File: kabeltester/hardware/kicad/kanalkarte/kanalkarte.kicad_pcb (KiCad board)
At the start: 6 copper layers, 118 x 74 mm, 413 parts, among them J1 DIN 41612 C96 Feder, J2 Messkarte, U1 SN74HC595PW, U10 CD74HCT4067M96, U11 ADG1606BRUZ, U12 CD74HCT4067M96, U13 ADG1606BRUZ, U14 CD74HCT4067M96, U15 ADG1606BRUZ, U16 CD74HCT4067M96, U17 ADG1606BRUZ, U18 CD74HCT4067M96, U2 SN74HC595PW, U3 ADG1606BRUZ, U4 CD74HCT4067M96, U5 ADG1606BRUZ, U6 CD74HCT4067M96, U7 ADG1606BRUZ, U8 CD74HCT4067M96, U9 ADG1606BRUZ

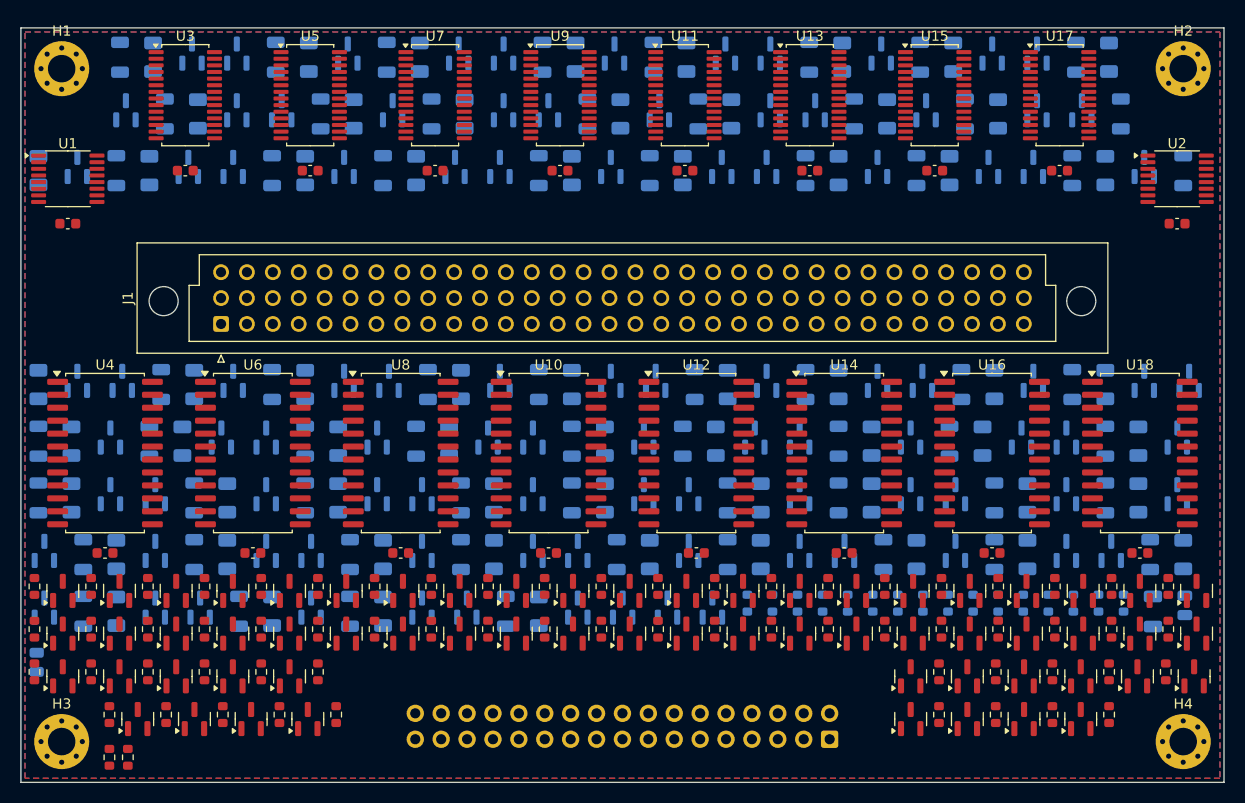
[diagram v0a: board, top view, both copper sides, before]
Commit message: Kanalkarte 6 Lagen, neue Platzierung: Zwischenstand Runde 1 (945 -> 180 offen)
Co-Authored-By: Claude Opus 5.5 <noreply@anthropic.com>
Claude-Session: https://claude.ai/code/session_0119zGeGQCWTR3UwpEi96iWe
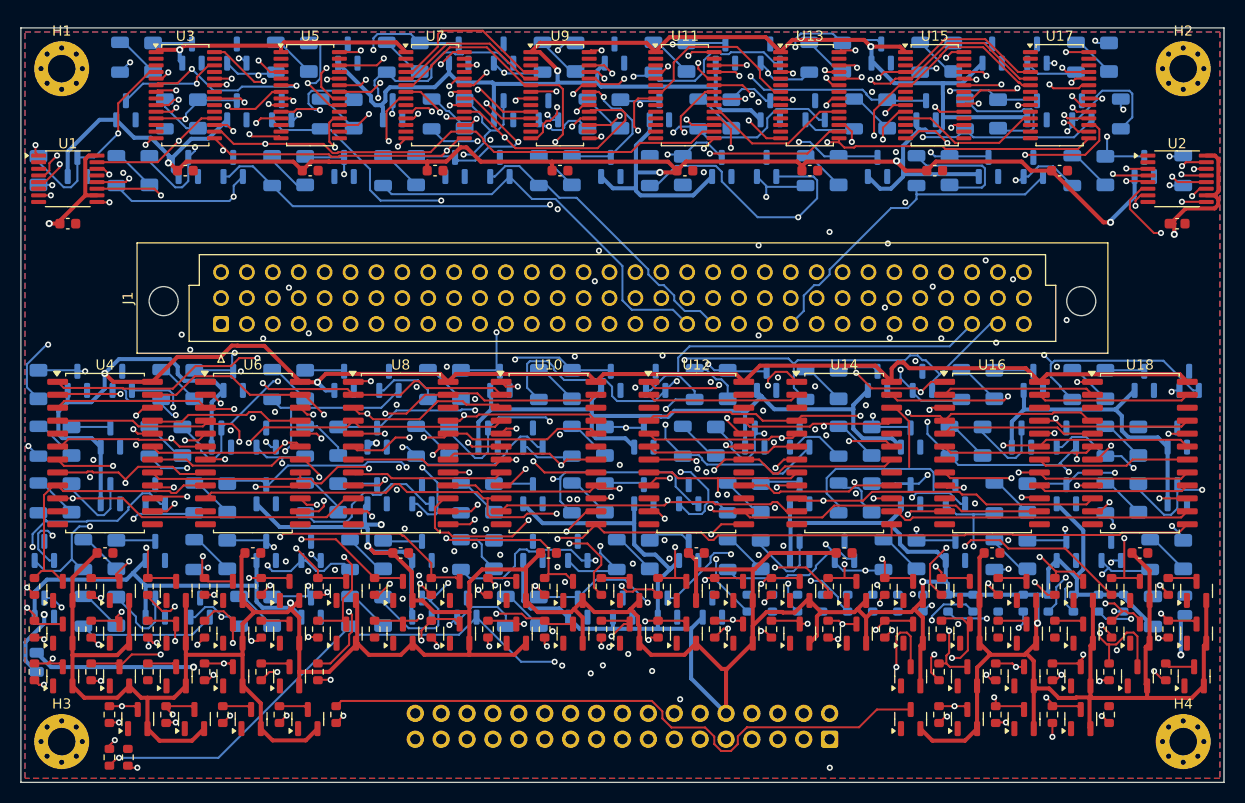
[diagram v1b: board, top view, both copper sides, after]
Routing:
- net 5VA: track 0.00 -> 1185.0 mm, vias 0 -> 15
- net 3V3: track 0.00 -> 239.8 mm, vias 0 -> 4
- net LA0: track 0.00 -> 233.7 mm, vias 0 -> 6
- net HA2: track 0.00 -> 221.1 mm, vias 0 -> 7
- net LA3: track 0.00 -> 194.4 mm, vias 0 -> 5
- net LA1: track 0.00 -> 190.4 mm, vias 0 -> 5
- net SR_LATCH: track 0.00 -> 182.7 mm, vias 0 -> 2
- net SR_CLK: track 0.00 -> 179.9 mm, vias 0 -> 2
- net LA2: track 0.00 -> 176.0 mm, vias 0 -> 5
- net TP34: track 0.00 -> 171.7 mm, vias 0 -> 4
- net HA0: track 0.00 -> 168.8 mm, vias 0 -> 6
- net TP52: track 0.00 -> 167.8 mm, vias 0 -> 4
- net TP51: track 0.00 -> 163.6 mm, vias 0 -> 5
- net S63: track 0.00 -> 160.5 mm, vias 0 -> 5
- net TP61: track 0.00 -> 160.1 mm, vias 0 -> 2
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
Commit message: Kanalkarte 6 Lagen, neue Platzierung: Zwischenstand Runde 2 (180 -> 167 offen)
Co-Authored-By: Claude Opus 5.5 <noreply@anthropic.com>
Claude-Session: https://claude.ai/code/session_0119zGeGQCWTR3UwpEi96iWe
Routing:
- net ENF_LO1: track 57.9 -> 206.1 mm, vias 2 -> 4
- net F43: track 8.02 -> 107.6 mm, vias 0 -> 5
- net TP45: track 15.9 -> 99.3 mm, vias 0 -> 2
- net HA0: track 168.8 -> 248.1 mm, vias 6 -> 7
- net F41: track 8.00 -> 78.8 mm, vias 0 -> 6
- net LA2: track 176.0 -> 225.6 mm, vias 5 -> 7
- net TP14: track 47.8 -> 91.2 mm, vias 1 -> 2
- net 5VA: track 1185.0 -> 1227.2 mm, vias 15 -> 17
- net TP9: track 57.7 -> 97.1 mm, vias 2 -> 5
- net S55: track 106.6 -> 144.5 mm, vias 3 -> 5
- net S5: track 22.8 -> 60.5 mm, vias 2 -> 4
- net LA0: track 233.7 -> 266.0 mm, vias 6 -> 8
- net HA1: track 152.7 -> 183.2 mm
- net F36: track 58.3 -> 87.4 mm, vias 2 -> 5
- net F12: track 41.9 -> 71.0 mm, vias 2 -> 4
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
